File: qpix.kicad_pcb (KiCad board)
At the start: 4 copper layers, 82.6 x 92.8 mm, 109 parts, among them J1 Conn_01x40, J10 VC, J11 Conn_Coaxial_Power, J13 DigReset, J2 Conn_01x09, J3 Conn_02x03, J4 Conn_02x03, J5 SPI, J6 Conn_02x03, J7 Conn_Coaxial, J8 Conn_02x03, J9 Conn_Coaxial_Power, Q1 Q_NMOS_GSD, Q2 Q_NMOS_GSD, Q3 Q_NMOS_GSD, Q4 Q_NMOS_GSD, U1 qpix_digital, U2 TPS73101DBV, U3 9DMV0141AKILF, U4 DS90C401M_NOPB

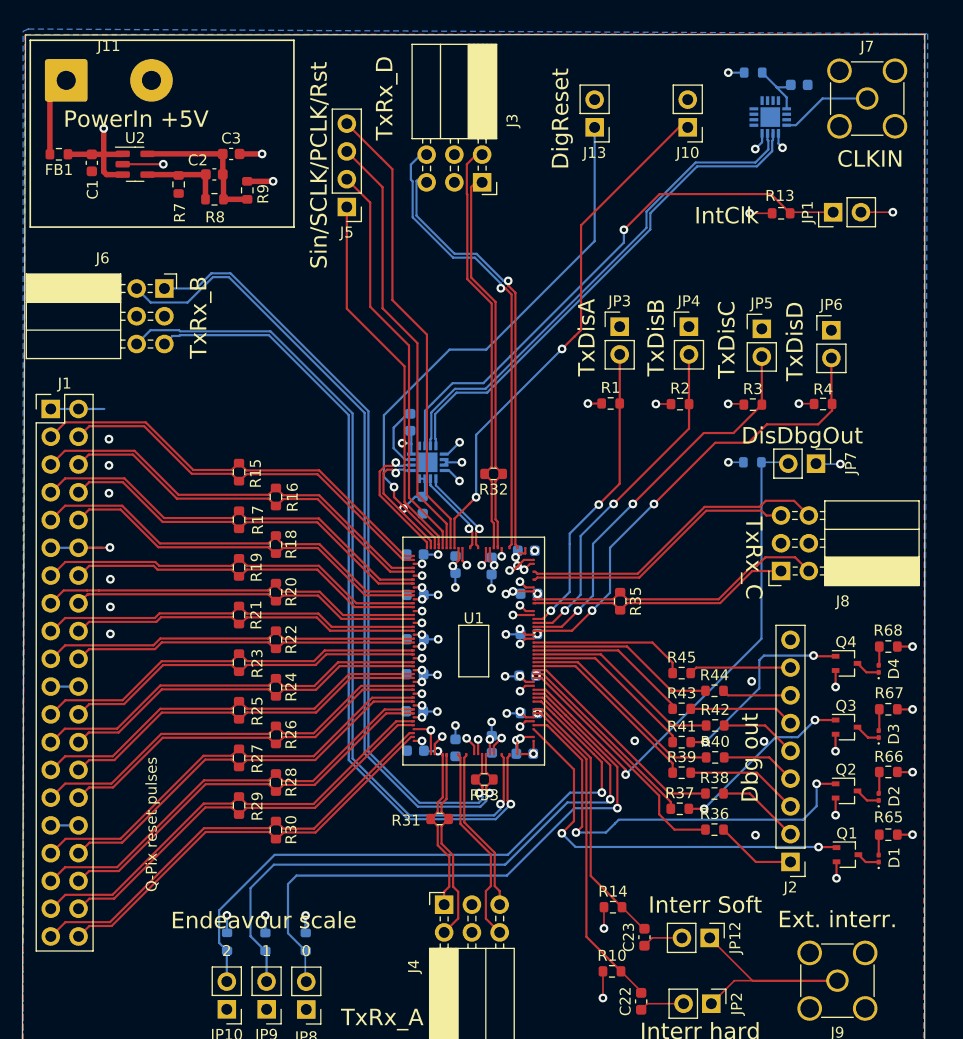
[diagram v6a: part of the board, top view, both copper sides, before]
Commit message: fix qpix ASIC pins (65,66) -> (VDD,GND)
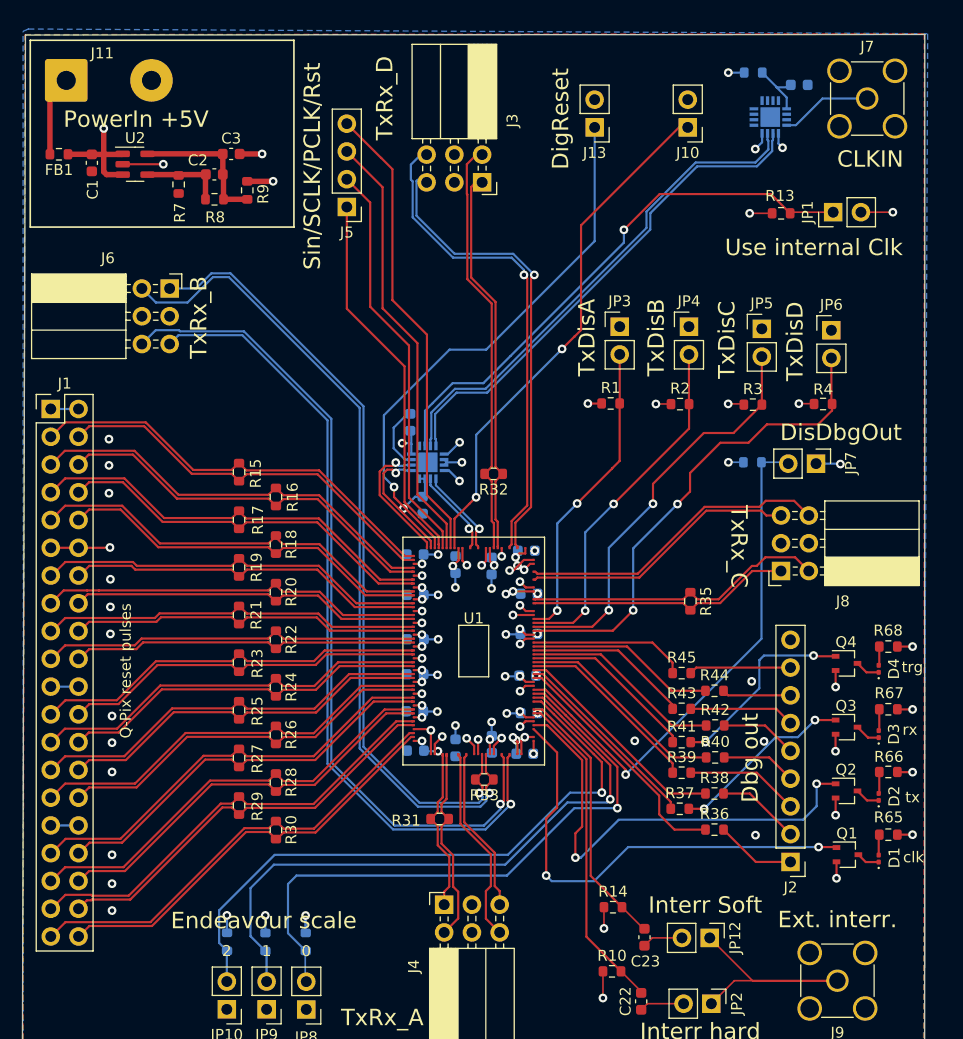
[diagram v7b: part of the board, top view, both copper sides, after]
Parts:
- moved R35 6.42 mm to (156.4, 101.3)
- moved J6 0.48 mm to (108.7, 72.7)
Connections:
- U1 pad 65: GND -> VDD
- U1 pad 66: VDD -> GND
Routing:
- net dbgClkDiv: track 37.2 -> 42.8 mm
- net GND: track 79.2 -> 74.8 mm, vias 51 -> 57
- net dbgDataValid: track 39.4 -> 42.8 mm
- net /DataoutD_N: track 42.5 -> 45.4 mm
- net /DataoutD_P: track 39.9 -> 42.7 mm
- net TxRxDisable_3: track 42.9 -> 44.8 mm
- net TxRxDisable_2: track 36.5 -> 38.1 mm
- net TxRxDisable_1: track 31.5 -> 32.6 mm
- net VDD: vias 50 -> 51
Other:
- board text added: "Use internal Clk"
- board text added: "clk"
- board text added: "rx"
- board text added: "trg"
- board text added: "tx"
- board text removed: "IntClk"

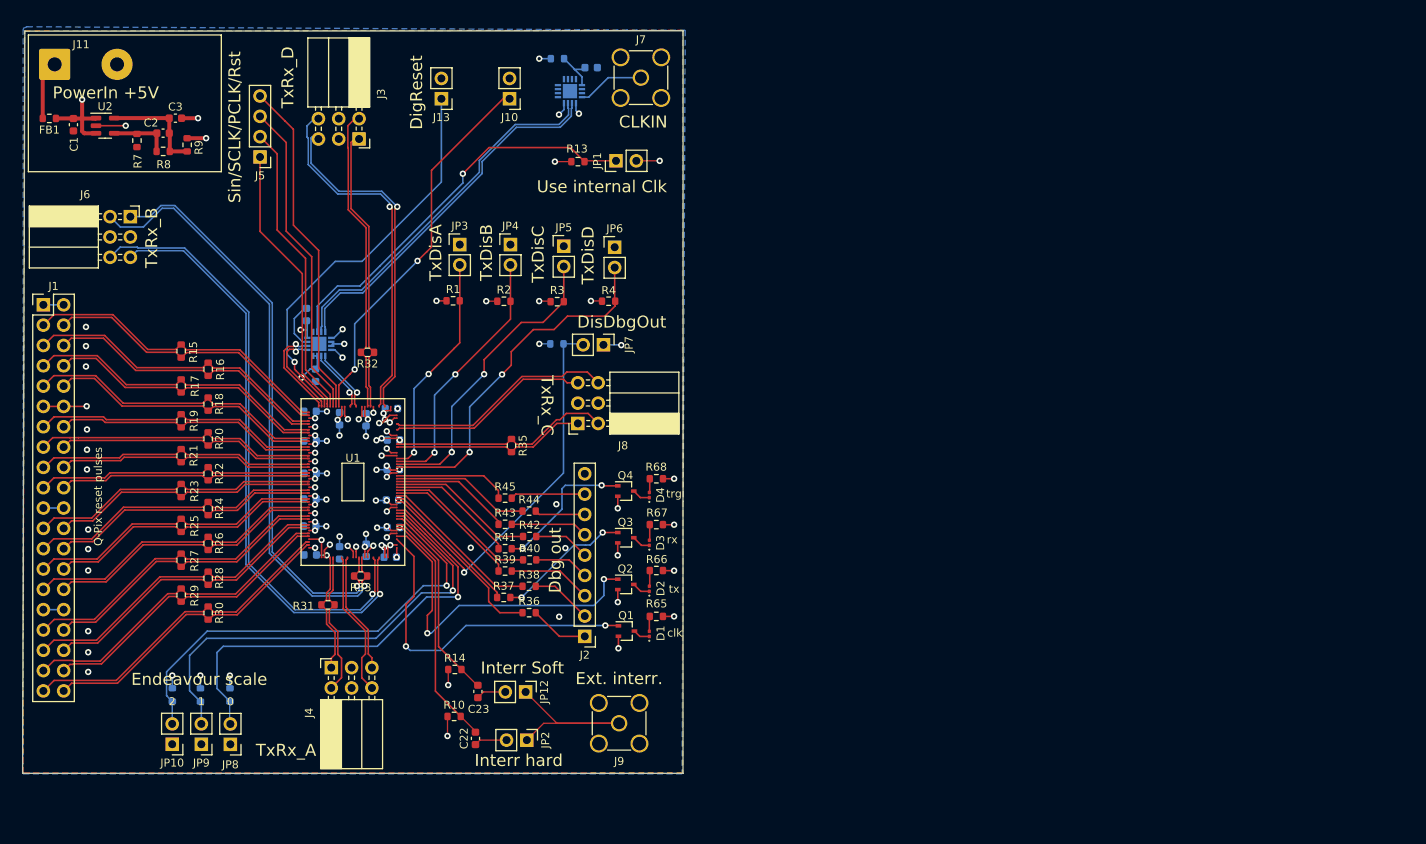
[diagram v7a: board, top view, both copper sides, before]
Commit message: trying to reroute new cob footprint
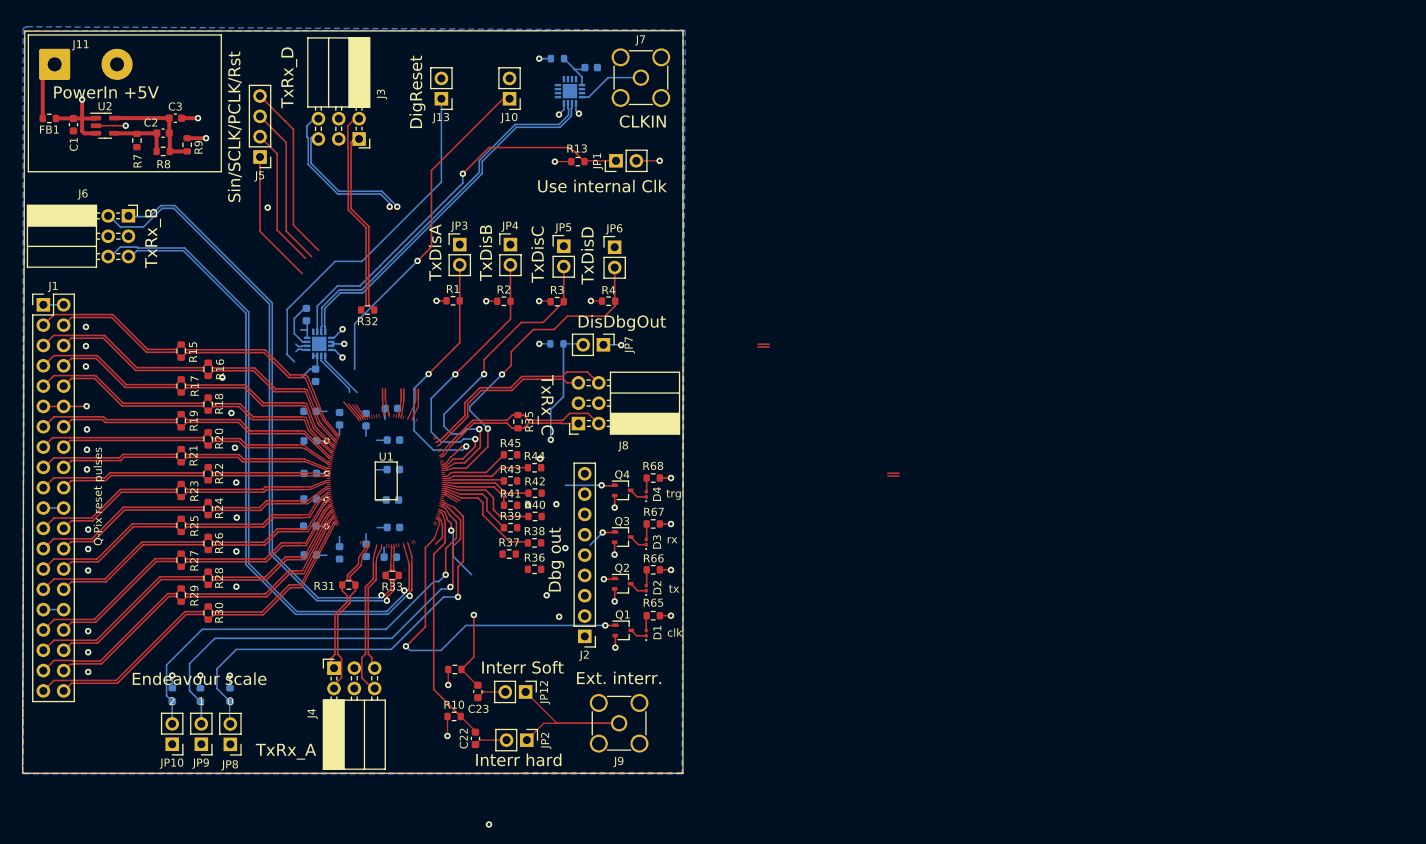
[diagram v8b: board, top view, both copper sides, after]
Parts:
- moved R45 5.46 mm to (156.2, 102.4)
- moved R36 5.46 mm to (159.2, 116.7)
- moved R37 5.46 mm to (156.1, 114.8)
- moved R38 5.46 mm to (159.2, 113.4)
- moved R39 5.46 mm to (156.2, 111.5)
- moved R40 5.46 mm to (159.3, 110.1)
- moved R41 5.46 mm to (156.2, 108.7)
- moved R42 5.46 mm to (159.3, 107.2)
- moved R43 5.46 mm to (156.2, 105.7)
- moved R44 5.46 mm to (159.2, 104.0)
- moved R32 5.29 mm to (138.4, 84.3)
- moved U1 4.17 mm to (140.7, 105.7)
- moved R33 3.94 mm to (141.4, 117.5)
- moved R31 3.60 mm to (136.0, 118.7)
- moved R35 3.09 mm to (157.2, 98.3)
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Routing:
- net dbgDataValid: track 42.8 -> 5.68 mm, vias 2 -> 1
- net disableDbgOut: track 48.1 -> 15.5 mm
- net VDD: track 78.8 -> 49.5 mm, vias 51 -> 16
- net GND: track 74.8 -> 47.2 mm, vias 57 -> 40
- net /DataoutD_N: track 45.4 -> 23.9 mm
- net /DataoutD_P: track 42.7 -> 21.3 mm
- net /SR_reset: track 42.8 -> 22.3 mm
- net Net-(U1-Pad79): track 22.5 -> 2.09 mm
- net /PCLK: track 40.1 -> 20.2 mm
- net /SCLK: track 37.4 -> 17.6 mm
- net /Sin: track 34.7 -> 18.8 mm
- net Net-(R37-Pad1): track 18.0 -> 2.39 mm
- net dbgRxValid: track 16.8 -> 4.11 mm
- net dbgInterr: track 18.1 -> 6.59 mm
- net dbgRxBusy: track 10.4 -> 0.00 mm
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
